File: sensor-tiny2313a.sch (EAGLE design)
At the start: 34 parts, among them IC1 TINY2313-*P*, IC2 L6920, K1 68611014422, M1 NRF24L01P-M, M2 DHT22, Q1 BC847CSMD

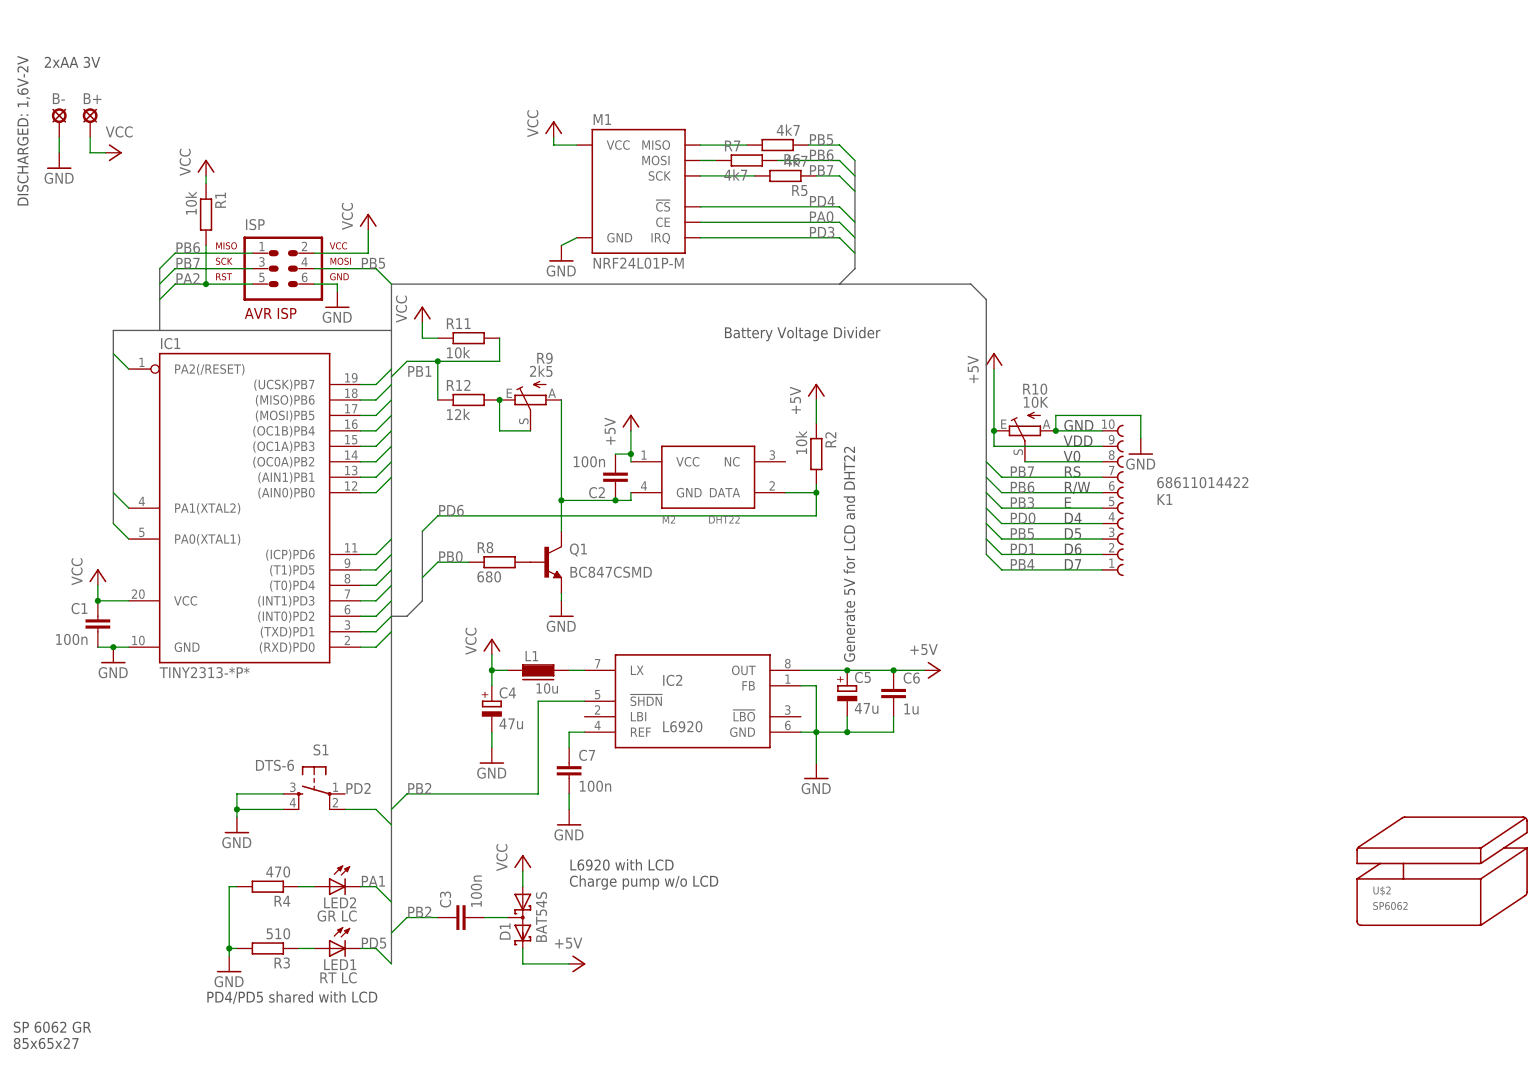
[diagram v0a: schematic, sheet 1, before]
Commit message: removed really complicating lcd from small version, layouted single sided pcb
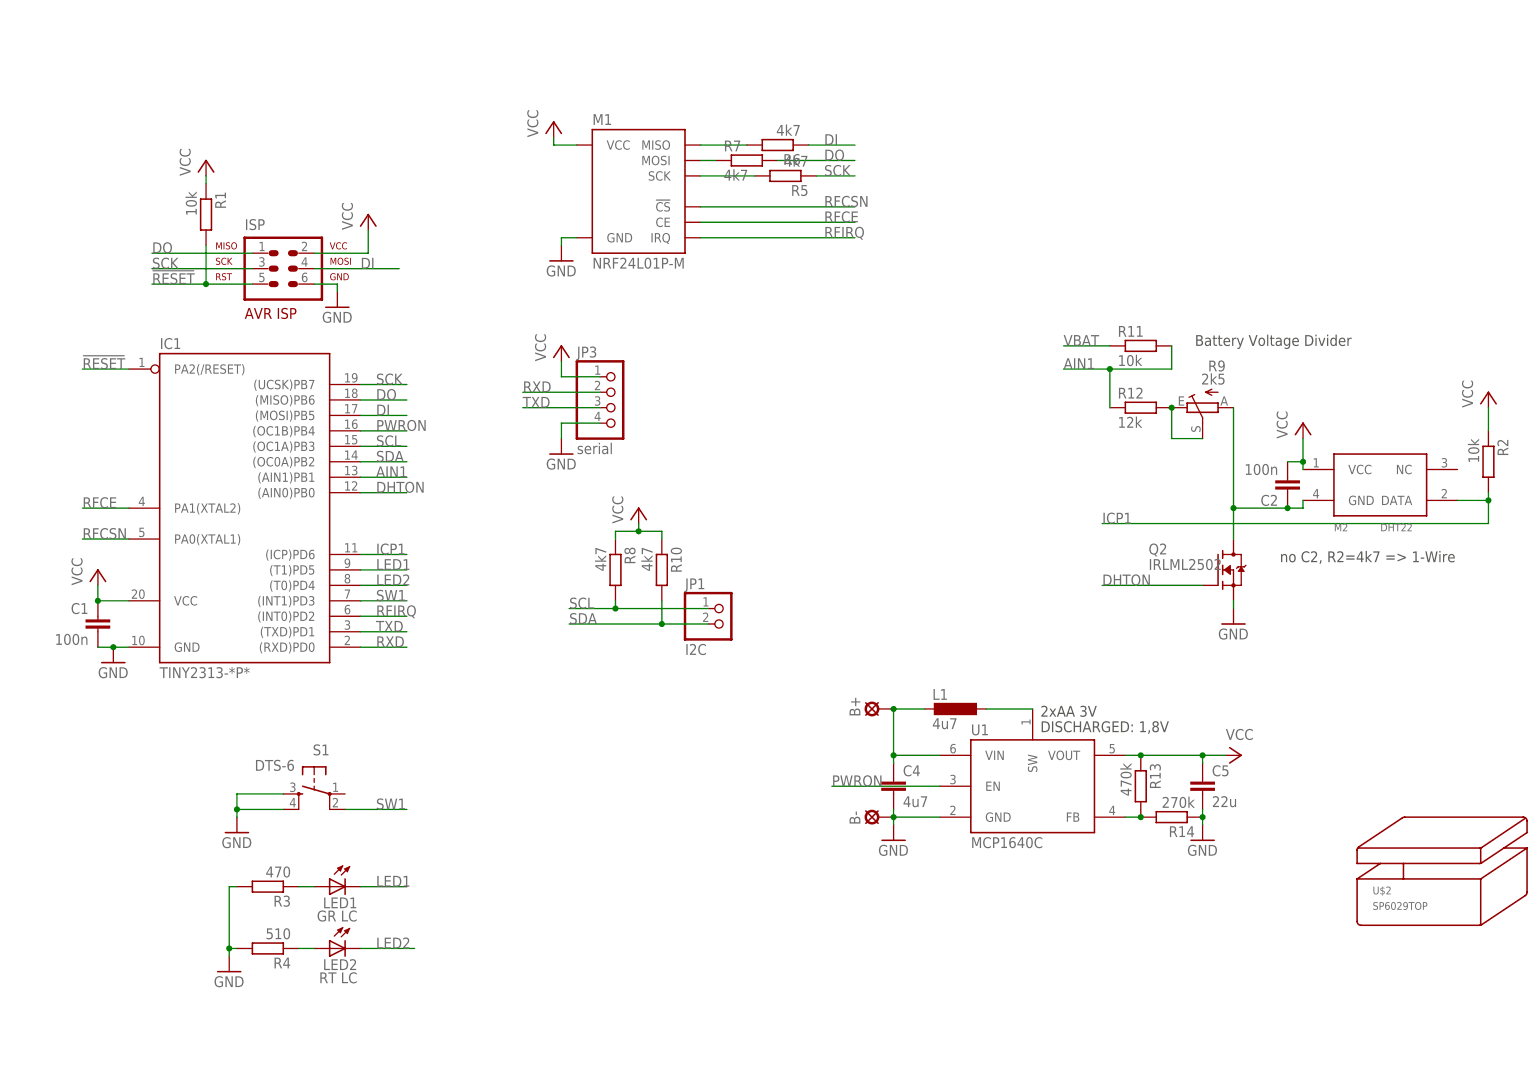
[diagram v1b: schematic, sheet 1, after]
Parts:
- removed C3, C7: 100n, rcl:C-EUC0805
- removed C6: 1u, rcl:C-EUC0805
- removed D1: BAT54S, diode:BAT54S
- removed IC2: L6920, l6920:L6920
- removed K1: 68611014422, Wuerth_Elektronik_eiCan_03_ZIF_Connectors_Flat_Flexible_Cable:68611014422
- removed Q1: BC847CSMD, transistor-npn:BC847CSMD
- added JP1: I2C, pinhead-mod:PINHD-1X2_2.54
- added JP3: serial, pinhead-mod:PINHD-1X4_2.54
- added Q2: IRLML2502, xmaker:IRLML2502
- added R13: 470k, rcl:R-EU_R0603
- added R14: 270k, rcl:R-EU_R0603
- added U1: MCP1640C, karlnet-parts:MCP1640
- C1, C2: device rcl:C-EUC0805 -> rcl:C-EUC0603
- C4: value 47u -> 4u7; device rcl:CPOL-EUE5-5 -> rcl:C-EUC0805; _REICHELT_ (none) -> X7R-G0805 4,7/16
- C5: value 47u -> 22u; device rcl:CPOL-EUE5-5 -> rcl:C-EUC1206; _REICHELT_ (none) -> X7R-G1206 22/10
- L1: value 10u -> 4u7; device fastron_07HCP:07HCP-10U -> inductor-Fastron:L-EUPISG; _REICHELT_ L-PISG 10µ -> L-PISG 4,7µ
- LED1: value RT LC -> GR LC; I 2mA -> 2.2mA; U_F 2V -> 2V2
- LED2: value GR LC -> RT LC; I 2.2mA -> 2mA; U_F 2V2 -> 2V
- R1, R11, R12, R2, R5, R6, R7: device rcl:R-EU_R0805 -> rcl:R-EU_R0603
- R10: value 10K -> 4k7; device pot:TRIM_EU-CA6H -> rcl:R-EU_R0603
- R3: value 510 -> 470; device rcl:R-EU_R0805 -> rcl:R-EU_R0603
- R4: value 470 -> 510; device rcl:R-EU_R0805 -> rcl:R-EU_R0603
- R8: value 680 -> 4k7; device rcl:R-EU_R0805 -> rcl:R-EU_R0603
- U$2: value SP6062 -> SP6029TOP; device strapubox:SP6062 -> strapubox:SP6029TOP
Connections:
- net N$3 renamed RSCK
- net N$4 renamed RDI
- net N$5 renamed RDO
- net PA2 renamed !RESET
- net PB1 renamed AIN1
- net PD5 renamed LED1
- net PD6 renamed ICP1
- removed net +5V: C2.2, C5.+, C6.1, D1.C2, IC2.OUT, K1.9, M2.VCC, R10.E, R2.1
- removed net N$10: IC2.LX, L1.2
- removed net N$11: C7.1, IC2.REF
- removed net N$12: K1.8, R10.S
- removed net N$14: C3.2, D1.C1A2
- removed net N$6: Q1.B, R8.2
- removed net PA0: IC1.PA0(XTAL1), M1.CE
- removed net PA1: IC1.PA1(XTAL2), LED2.C
- removed net PB0: IC1.(AIN0)PB0, R8.1
- removed net PB2: C3.1, IC1.(OC0A)PB2, IC2.!SHDN
- removed net PB3: IC1.(OC1A)PB3, K1.5
- removed net PB4: IC1.(OC1B)PB4, K1.1
- removed net PB5: IC1.(MOSI)PB5, ISP.4, K1.3, R6.1
- removed net PB6: IC1.(MISO)PB6, ISP.1, K1.6, R7.2
- removed net PB7: IC1.(UCSK)PB7, ISP.3, K1.7, R5.1
- removed net PD0: IC1.(RXD)PD0, K1.4
- removed net PD1: IC1.(TXD)PD1, K1.2
- removed net PD2: IC1.(INT0)PD2, S1.2
- removed net PD3: IC1.(INT1)PD3, M1.IRQ
- removed net PD4: IC1.(T0)PD4, M1.!CS
- new net DHTON: IC1.(AIN0)PB0, Q2.G
- new net DI: IC1.(MOSI)PB5, ISP.4, R6.1
- new net DO: IC1.(MISO)PB6, ISP.1, R7.2
- new net LED2: IC1.(T0)PD4, LED2.C
- new net N$8: L1.1, U1.SW
- new net N$9: R13.2, R14.2, U1.FB
- new net PWRON: IC1.(OC1B)PB4, U1.EN
- new net RFCE: IC1.PA1(XTAL2), M1.CE
- new net RFCSN: IC1.PA0(XTAL1), M1.!CS
- new net RFIRQ: IC1.(INT0)PD2, M1.IRQ
- new net RXD: IC1.(RXD)PD0, JP3.2
- new net SCK: IC1.(UCSK)PB7, ISP.3, R5.1
- new net SCL: IC1.(OC1A)PB3, JP1.1, R8.2
- new net SDA: IC1.(OC0A)PB2, JP1.2, R10.2
- new net SW1: IC1.(INT1)PD3, S1.2
- new net TXD: IC1.(TXD)PD1, JP3.3
- new net VBAT: B+.MP, C4.1, L1.2, R11.1, U1.VIN
- net GND: now also C4.2, C5.2, JP3.4, Q2.S, R14.1, U1.GND; no longer C4.-, C5.-, C6.2, C7.2, IC2.FB, IC2.GND, K1.10, Q1.E, R10.A
- net N$2: now also Q2.D; no longer Q1.C
- net VCC: now also C2.2, C5.1, JP3.1, M2.VCC, R10.1, R13.1, R2.1, R8.1, U1.VOUT; no longer B+.MP, C4.+, D1.A1, L1.1, R11.1
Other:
- note added: "DISCHARGED: 1,8V"
- note added: "no C2, R2=4k7 => 1-Wire"
- note removed: "D4"
- note removed: "D5"
- note removed: "D6"
- note removed: "D7"
- note removed: "DISCHARGED: 1,6V-2V"
- note removed: "E"
- note removed: "GND"
- note removed: "Generate 5V for LCD and DHT22"
- note removed: "L6920 with LCD Charge pump w/o LCD"
- note removed: "PD4/PD5 shared with LCD"
- note removed: "R/W"
- note removed: "RS"
- note removed: "SP 6062 GR 85x65x27"
- note removed: "V0"
- note removed: "VDD"
- moved on the sheet: B+, B-, C2, LED1, LED2, M2, R11, R12, R2, R3, R4, R8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

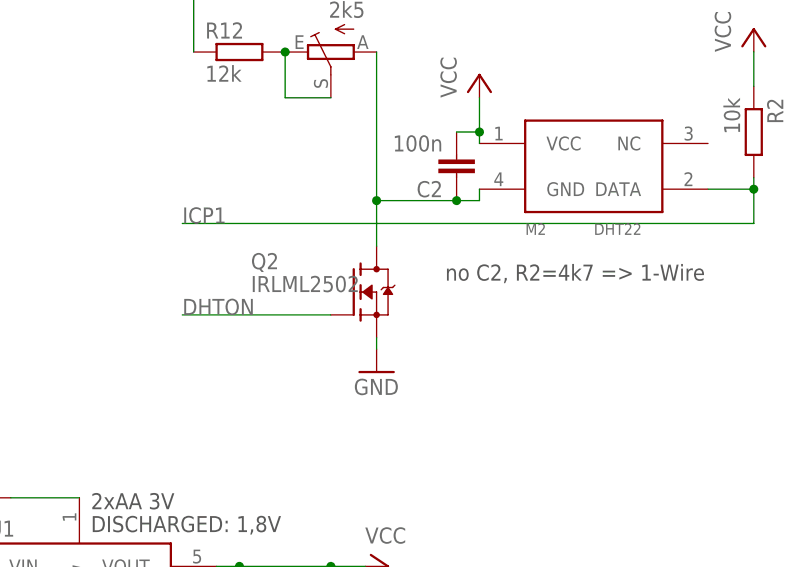
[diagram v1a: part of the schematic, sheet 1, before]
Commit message: changed irlml* parts to own library with better footprint
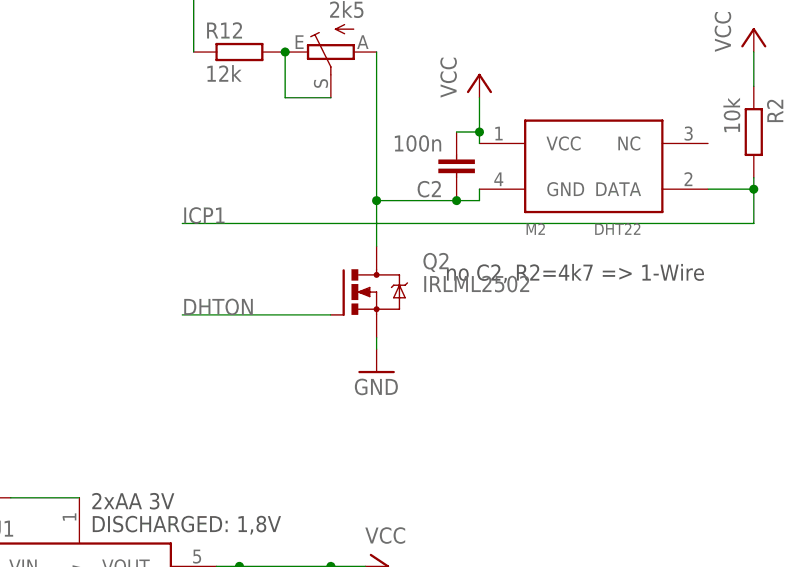
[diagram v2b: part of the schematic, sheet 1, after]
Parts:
- Q2: device xmaker:IRLML2502 -> mosfet:IRLML2502
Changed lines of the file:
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@@
 <setting verticaltext="up"/>
 </settings>
-<grid distance="1.27" unitdist="mm" unit="mm" style="lines" multiple="1" display="yes" altdistance="635" altunitdist="mic" altunit="mic"/>
+<grid distance="0.1" unitdist="inch" unit="mm" style="lines" multiple="1" display="yes" altdistance="0.01" altunitdist="inch" altunit="mm"/>
 <layers>
-<layer number="1" name="Top" color="4" fill="1" visible="yes" active="no"/>
-<layer number="2" name="Route2" color="1" fill="3" visible="yes" active="no"/>
-<layer number="3" name="Route3" color="4" fill="3" visible="yes" active="no"/>
-<layer number="4" name="Route4" color="1" fill="4" visible="yes" active="no"/>
-<layer number="5" name="Route5" color="4" fill="4" visible="yes" active="no"/>
-<layer number="6" name="Route6" color="1" fill="8" visible="yes" active="no"/>
-<layer number="7" name="Route7" color="4" fill="8" visible="yes" active="no"/>
-<layer number="8" name="Route8" color="1" fill="2" visible="yes" active="no"/>
-<layer number="9" name="Route9" color="4" fill="2" visible="yes" active="no"/>
-<layer number="10" name="Route10" color="1" fill="7" visible="yes" active="no"/>
-<layer number="11" name="Route11" color="4" fill="7" visible="yes" active="no"/>
-<layer number="12" name="Route12" color="1" fill="5" visible="yes" active="no"/>
-<layer number="13" name="Route13" color="4" fill="5" visible="yes" active="no"/>
-<layer number="14" name="Route14" color="1" fill="6" visible="yes" active="no"/>
-<layer number="15" name="Route15" color="4" fill="6" visible="yes" active="no"/>
-<layer number="16" name="Bottom" color="1" fill="1" visible="yes" active="no"/>
-<layer number="17" name="Pads" color="2" fill="1" visible="yes" active="no"/>
-<layer number="18" name="Vias" color="2" fill="1" visible="yes" active="no"/>
-<layer number="19" name="Unrouted" color="6" fill="1" visible="yes" active="no"/>
-<layer number="20" name="Dimension" color="15" fill="1" visible="yes" active="no"/>
-<layer number="21" name="tPlace" color="7" fill="1" visible="yes" active="no"/>
-<layer number="22" name="bPlace" color="7" fill="1" visible="yes" active="no"/>
-<layer number="23" name="tOrigins" color="15" fill="1" visible="yes" active="no"/>
-<layer number="24" name="bOrigins" color="15" fill="1" visible="yes" active="no"/>
-<layer number="25" name="tNames" color="7" fill="1" visible="yes" active="no"/>
-<layer number="26" name="bNames" color="7" fill="1" visible="yes" active="no"/>
-<layer number="27" name="tValues" color="7" fill="1" visible="yes" active="no"/>
-<layer number="28" name="bValues" color="7" fill="1" visible="yes" active="no"/>
+<layer number="1" name="Top" color="4" fill="1" visible="no" active="no"/>
+<layer number="2" name="Route2" color="1" fill="3" visible="no" active="no"/>
+<layer number="3" name="Route3" color="4" fill="3" visible="no" active="no"/>
+<layer number="4" name="Route4" color="1" fill="4" visible="no" active="no"/>
+<layer number="5" name="Route5" color="4" fill="4" visible="no" active="no"/>
+<layer number="6" name="Route6" color="1" fill="8" visible="no" active="no"/>
+<layer number="7" name="Route7" color="4" fill="8" visible="no" active="no"/>
+<layer number="8" name="Route8" color="1" fill="2" visible="no" active="no"/>
+<layer number="9" name="Route9" color="4" fill="2" visible="no" active="no"/>
+<layer number="10" name="Route10" color="1" fill="7" visible="no" active="no"/>
+<layer number="11" name="Route11" color="4" fill="7" visible="no" active="no"/>
+<layer number="12" name="Route12" color="1" fill="5" visible="no" active="no"/>
+<layer number="13" name="Route13" color="4" fill="5" visible="no" active="no"/>
+<layer number="14" name="Route14" color="1" fill="6" visible="no" active="no"/>
+<layer number="15" name="Route15" color="4" fill="6" visible="no" active="no"/>
+<layer number="16" name="Bottom" color="1" fill="1" visible="no" active="no"/>
+<layer number="17" name="Pads" color="2" fill="1" visible="no" active="no"/>
+<layer number="18" name="Vias" color="2" fill="1" visible="no" active="no"/>
+<layer number="19" name="Unrouted" color="6" fill="1" visible="no" active="no"/>
+<layer number="20" name="Dimension" color="15" fill="1" visible="no" active="no"/>
+<layer number="21" name="tPlace" color="7" fill="1" visible="no" active="no"/>
+<layer number="22" name="bPlace" color="7" fill="1" visible="no" active="no"/>
+<layer number="23" name="tOrigins" color="15" fill="1" visible="no" active="no"/>
+<layer number="24" name="bOrigins" color="15" fill="1" visible="no" active="no"/>
+<layer number="25" name="tNames" color="7" fill="1" visible="no" active="no"/>
+<layer number="26" name="bNames" color="7" fill="1" visible="no" active="no"/>
+<layer number="27" name="tValues" color="7" fill="1" visible="no" active="no"/>
+<layer number="28" name="bValues" color="7" fill="1" visible="no" active="no"/>
 <layer number="29" name="tStop" color="7" fill="3" visible="no" active="no"/>
 <layer number="30" name="bStop" color="7" fill="6" visible="no" active="no"/>
@@
 <layer number="35" name="tGlue" color="7" fill="4" visible="no" active="no"/>
 <layer number="36" name="bGlue" color="7" fill="5" visible="no" active="no"/>
-<layer number="37" name="tTest" color="7" fill="1" visible="yes" active="no"/>
-<layer number="38" name="bTest" color="7" fill="1" visible="yes" active="no"/>
+<layer number="37" name="tTest" color="7" fill="1" visible="no" active="no"/>
+<layer number="38" name="bTest" color="7" fill="1" visible="no" active="no"/>
 <layer number="39" name="tKeepout" color="4" fill="11" visible="no" active="no"/>
 <layer number="40" name="bKeepout" color="1" fill="11" visible="no" active="no"/>
@@
 <layer number="44" name="Drills" color="7" fill="1" visible="no" active="no"/>
 <layer number="45" name="Holes" color="7" fill="1" visible="no" active="no"/>
-<layer number="46" name="Milling" color="3" fill="1" visible="yes" active="no"/>
-<layer number="47" name="Measures" color="7" fill="1" visible="yes" active="no"/>
-<layer number="48" name="Document" color="7" fill="1" visible="yes" active="no"/>
-<layer number="49" name="Reference" color="7" fill="1" visible="yes" active="no"/>
-<layer number="50" name="dxf" color="7" fill="1" visible="yes" active="no"/>
-<layer number="51" name="tDocu" color="7" fill="1" visible="yes" active="no"/>
-<layer number="52" name="bDocu" color="7" fill="1" visible="yes" active="no"/>
-<layer number="53" name="tGND_GNDA" color="7" fill="9" visible="yes" active="no"/>
-<layer number="54" name="bGND_GNDA" color="1" fill="9" visible="yes" active="no"/>
-<layer number="56" name="wert" color="7" fill="1" visible="yes" active="no"/>
+<layer number="46" name="Milling" color="3" fill="1" visible="no" active="no"/>
+<layer number="47" name="Measures" color="7" fill="1" visible="no" active="no"/>
+<layer number="48" name="Document" color="7" fill="1" visible="no" active="no"/>
+<layer number="49" name="Reference" color="7" fill="1" visible="no" active="no"/>
+<layer number="50" name="dxf" color="7" fill="1" visible="no" active="no"/>
+<layer number="51" name="tDocu" color="7" fill="1" visible="no" active="no"/>
+<layer number="52" name="bDocu" color="7" fill="1" visible="no" active="no"/>
+<layer number="53" name="tGND_GNDA" color="7" fill="9" visible="no" active="no"/>
+<layer number="54" name="bGND_GNDA" color="1" fill="9" visible="no" active="no"/>
+<layer number="56" name="wert" color="7" fill="1" visible="no" active="no"/>
 <layer number="91" name="Nets" color="2" fill="1" visible="yes" active="yes"/>
 <layer number="92" name="Busses" color="1" fill="1" visible="yes" active="yes"/>
@@
 <part name="P+2" library="supply1" deviceset="VCC" device=""/>
 <part name="GND1" library="supply1" deviceset="GND" device=""/>
-<part name="Q2" library="xmaker" deviceset="IRLML2502" device=""/>
+<part name="Q2" library="mosfet" deviceset="IRLML2502" device=""/>
 <part name="P+3" library="supply1" deviceset="VCC" device=""/>
 <part name="P+7" library="supply1" deviceset="VCC" device=""/>

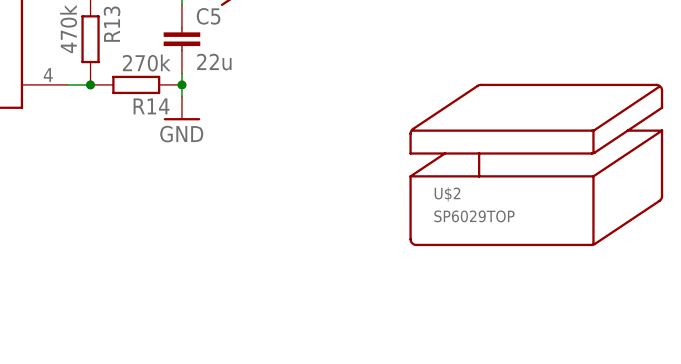
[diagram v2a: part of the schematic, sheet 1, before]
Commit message: cc-by-sa license
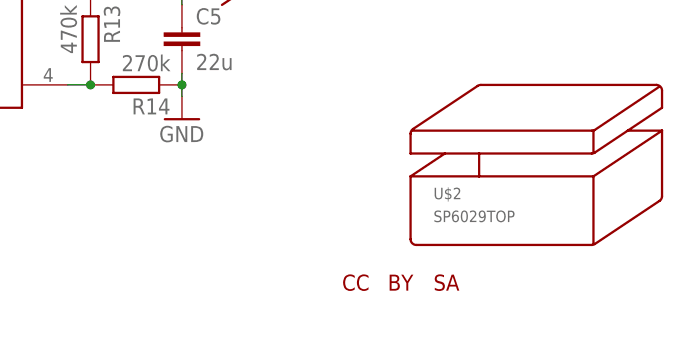
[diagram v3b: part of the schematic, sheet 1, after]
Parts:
- added U$1: CC-TOP-HALF, creative-commons:CC-TOP-HALF
- added U$3: BY-TOP-HALF, creative-commons:BY-TOP-HALF
- added U$4: SA-TOP-HALF, creative-commons:SA-TOP-HALF
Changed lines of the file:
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@@
 <part name="P+9" library="supply1" deviceset="VCC" device=""/>
 <part name="GND5" library="supply1" deviceset="GND" device=""/>
+<part name="U$1" library="creative-commons" deviceset="CC" device="-TOP-HALF"/>
+<part name="U$3" library="creative-commons" deviceset="BY" device="-TOP-HALF"/>
+<part name="U$4" library="creative-commons" deviceset="SA" device="-TOP-HALF"/>
 </parts>
 <sheets>
@@
 <instance part="P+9" gate="VCC" x="95.25" y="120.65"/>
 <instance part="GND5" gate="1" x="95.25" y="102.87"/>
+<instance part="U$1" gate="G$1" x="218.44" y="20.32"/>
+<instance part="U$3" gate="G$1" x="223.52" y="20.32"/>
+<instance part="U$4" gate="G$1" x="228.6" y="20.32"/>
 </instances>
 <busses>
